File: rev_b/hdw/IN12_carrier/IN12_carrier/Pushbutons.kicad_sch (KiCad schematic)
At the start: 55 parts, among them U2203 74LVC1G17

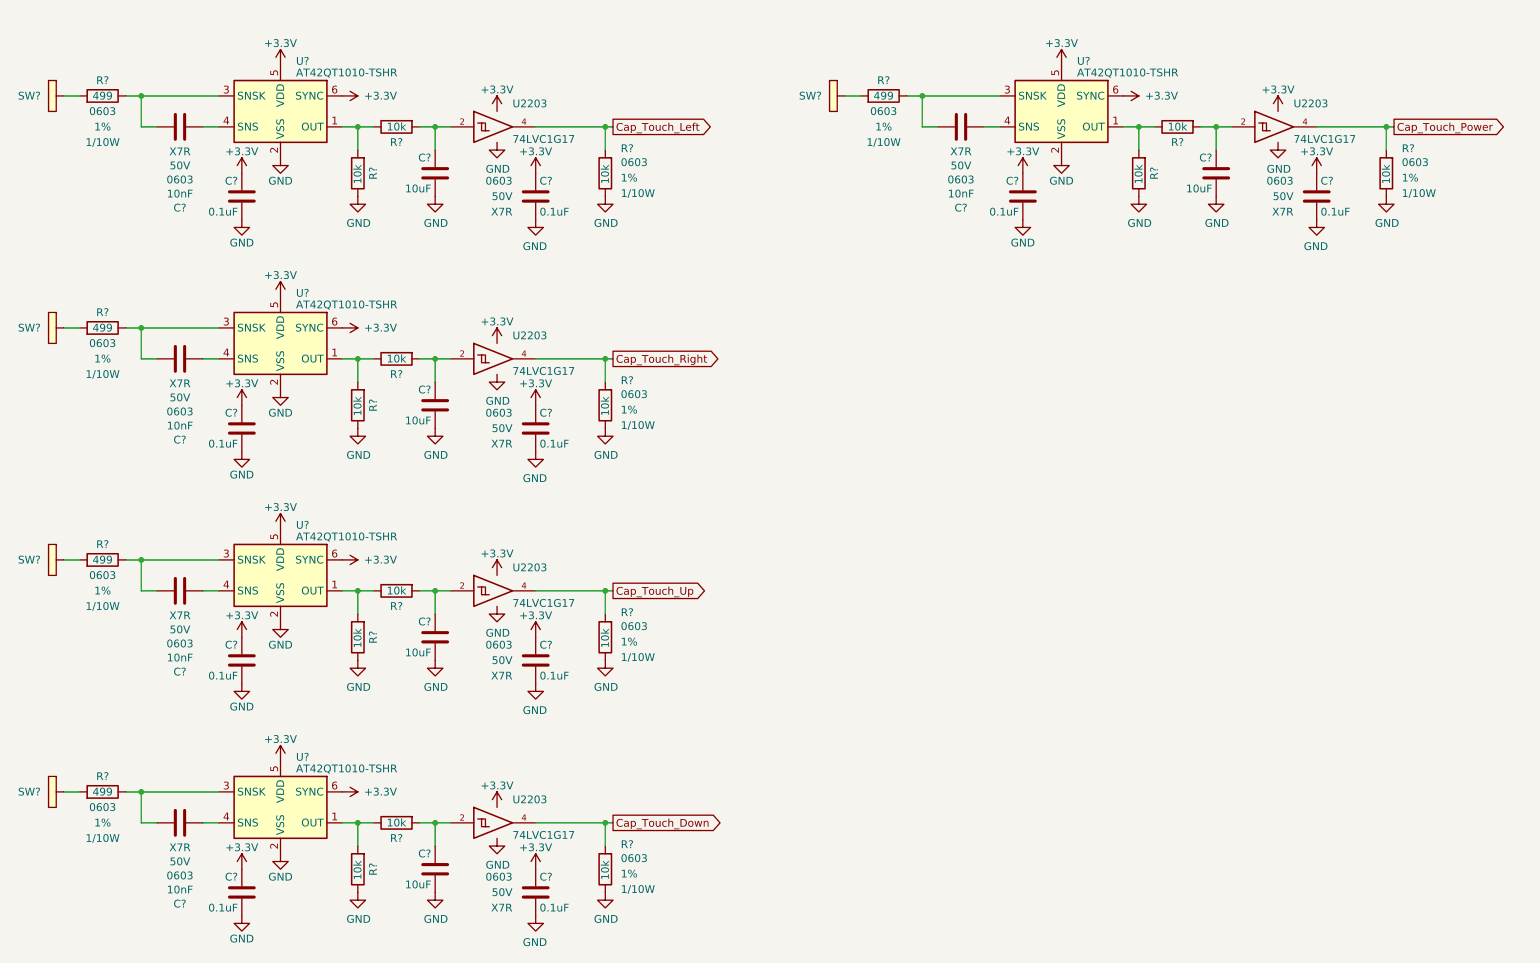
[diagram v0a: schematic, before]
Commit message: updated footprints, ran some DRC
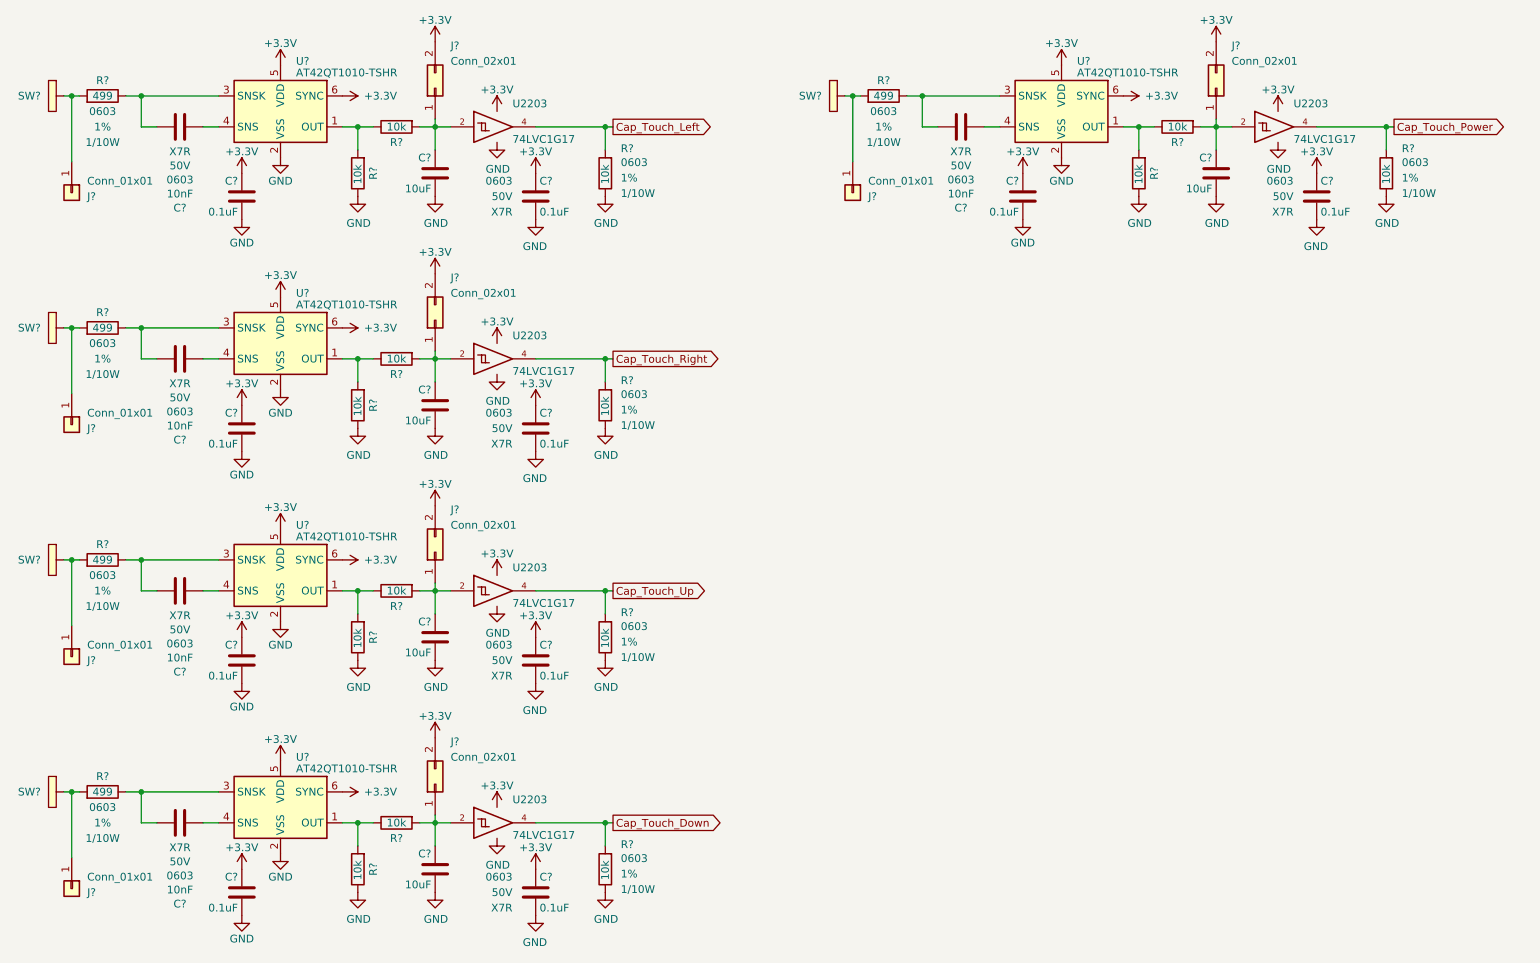
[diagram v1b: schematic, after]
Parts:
- added J? (x5): Conn_02x01, symbol Connector_Generic:Conn_02x01
- added J? (x5): Conn_01x01, symbol Connector_Generic:Conn_01x01
- C? (x10): Digi-Key PN 399-7845-1-ND -> (none)
- C? (x5): Digi-Key PN 490-10474-1-ND -> (none)
- C? (x5): Digi-Key PN 399-7842-1-ND -> (none)
- R? (x5): Digi-Key PN RMCF0603FT499RCT-ND -> (none)
- R? (x15): Digi-Key PN YAG2321CT-ND -> (none)
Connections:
- net +3V3: now also J?.2 (Pin_2), J?.2 (Pin_2), J?.2 (Pin_2), J?.2 (Pin_2), J?.2 (Pin_2)
- net at C?.1, R?.1, U2203.2: now also J?.1 (Pin_1) (x5)
- net at R?.1, SW?.1 (TP): now also J?.1 (Pin_1) (x5)
